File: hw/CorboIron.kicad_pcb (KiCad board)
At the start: 2 copper layers, 78.7 x 99.1 mm, 101 parts, among them P1 CONN_01X03, P10 CONN_01X04, P11 CONN_01X04, P2 CONN_01X03, P3 CONN_01X03, P4 Arduino_nano, P5 CONN_01X03, P6 CONN_01X04, P7 CONN_01X02, P8 CONN_01X03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

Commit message: Added descriptive text in silk
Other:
- board text added: "Four channel solder iron controller"
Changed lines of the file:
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@@
     (area 116.684238 56.84 211.2 163.905001)
     (thickness 1.6)
-    (drawings 29)
+    (drawings 30)
     (tracks 1597)
     (zones 0)
@@
   )
   (setup
-    (last_trace_width 0.3)
+    (last_trace_width 0.25)
     (user_trace_width 0.1524)
     (user_trace_width 0.3)
@@
     )
   )
+  (gr_text "Four channel \nsolder iron controller" (at 147.32 94.742) (layer F.SilkS)
+    (effects (font (size 1.5 1.5) (thickness 0.3)))
+  )
   (gr_text "LEDS INDICATE OVER HEAT PROTECTION" (at 139.7 161.798) (layer F.SilkS)

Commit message: Minor changes
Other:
- board text added: "1"
- board text added: "2"
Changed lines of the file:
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@@
     (area 116.684238 56.84 211.2 163.905001)
     (thickness 1.6)
-    (drawings 30)
-    (tracks 1597)
+    (drawings 32)
+    (tracks 1598)
     (zones 0)
     (modules 101)
@@
   (layers
     (0 F.Cu signal)
-    (31 B.Cu signal hide)
+    (31 B.Cu signal)
     (32 B.Adhes user)
     (33 F.Adhes user)
@@
   )
   (setup
-    (last_trace_width 0.25)
+    (last_trace_width 1)
     (user_trace_width 0.1524)
     (user_trace_width 0.3)
@@
     )
   )
+  (gr_text 2 (at 119.634 162.56) (layer B.Cu)
+    (effects (font (size 1.5 1.5) (thickness 0.3)))
+  )
+  (gr_text 1 (at 118.11 162.56) (layer F.Cu)
+    (effects (font (size 1.5 1.5) (thickness 0.3)))
+  )
   (gr_text "Four channel \nsolder iron controller" (at 147.32 94.742) (layer F.SilkS)
     (effects (font (size 1.5 1.5) (thickness 0.3)))
   )
-  (gr_text "LEDS INDICATE OVER HEAT PROTECTION" (at 139.7 161.798) (layer F.SilkS)
+  (gr_text "LEDS INDICATE OVER HEAT PROTECTION" (at 150.368 161.798) (layer F.SilkS)
     (effects (font (size 1.5 1.5) (thickness 0.3)))
   )
@@
   (via (at 131.445 142.621) (size 0.6) (drill 0.4) (layers F.Cu B.Cu) (net 1))
   (segment (start 129.286 142.621) (end 131.445 142.621) (width 0.7) (layer B.Cu) (net 1))
-  (segment (start 154.178 138.496) (end 154.178 133.223) (width 0.7) (layer F.Cu) (net 1))
-  (segment (start 148.717 131.191) (end 144.78 127.254) (width 0.7) (layer B.Cu) (net 1))
-  (segment (start 152.146 131.191) (end 148.717 131.191) (width 0.7) (layer B.Cu) (net 1))
-  (segment (start 154.178 133.223) (end 152.146 131.191) (width 0.7) (layer B.Cu) (net 1))
+  (segment (start 154.178 138.496) (end 154.178 135.636) (width 1) (layer F.Cu) (net 1))
   (via (at 154.178 133.223) (size 0.6) (drill 0.4) (layers F.Cu B.Cu) (net 1))
+  (segment (start 154.178 133.223) (end 152.146 131.191) (width 1) (layer B.Cu) (net 1))
+  (segment (start 152.146 131.191) (end 148.717 131.191) (width 1) (layer B.Cu) (net 1))
+  (segment (start 148.717 131.191) (end 144.78 127.254) (width 1) (layer B.Cu) (net 1))
+  (segment (start 154.178 135.636) (end 154.178 133.223) (width 0.7) (layer F.Cu) (net 1))
   (via (at 134.874 127.254) (size 0.6) (drill 0.4) (layers F.Cu B.Cu) (net 1))
   (segment (start 134.874 127.254) (end 134.874 131.572) (width 0.7) (layer B.Cu) (net 1))
@@
   (via (at 148.336 137.16) (size 0.6) (drill 0.4) (layers F.Cu B.Cu) (net 1))
   (segment (start 148.336 137.16) (end 148.27 137.16) (width 0.3) (layer F.Cu) (net 1))
-  (segment (start 153.538 138.496) (end 151.826 140.208) (width 0.7) (layer F.Cu) (net 1))
+  (segment (start 153.538 138.496) (end 151.826 140.208) (width 1) (layer F.Cu) (net 1))
   (via (at 151.826 140.208) (size 0.6) (drill 0.4) (layers F.Cu B.Cu) (net 1))
   (segment (start 151.826 140.208) (end 148.778 137.16) (width 0.3) (layer B.Cu) (net 1))
@@
     (polygon
       (pts
-        (xy 116.84 64.77) (xy 116.84 163.83) (xy 148.336 163.83) (xy 148.336 131.826) (xy 176.784 131.826)
-        (xy 176.784 163.83) (xy 195.58 163.83) (xy 195.58 64.77) (xy 176.784 64.77) (xy 176.784 95.504)
-        (xy 148.336 95.504) (xy 148.336 64.77)
+        (xy 116.84 64.77) (xy 116.84 160.782) (xy 120.65 160.782) (xy 120.65 163.83) (xy 148.336 163.83)
+        (xy 148.336 131.826) (xy 176.784 131.826) (xy 176.784 163.83) (xy 195.58 163.83) (xy 195.58 64.77)
+        (xy 176.784 64.77) (xy 176.784 95.504) (xy 148.336 95.504) (xy 148.336 64.77)
       )
     )

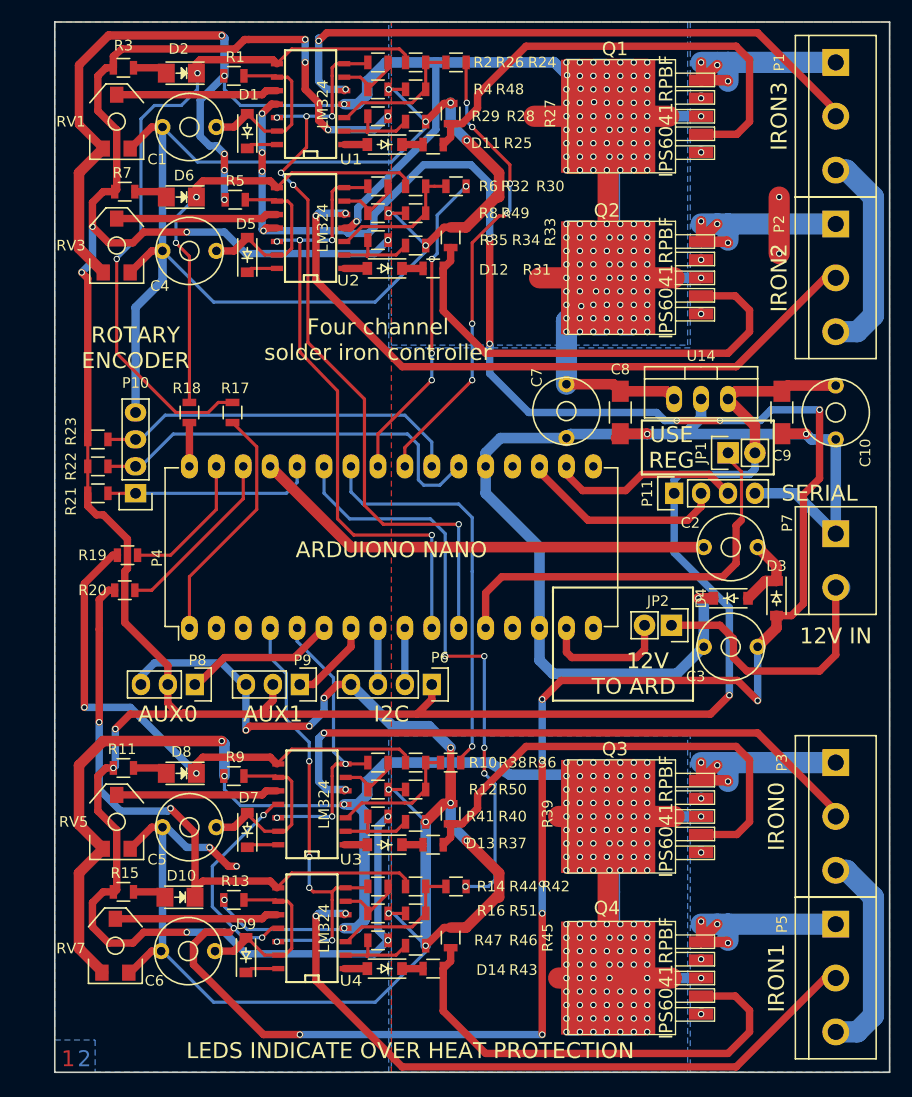
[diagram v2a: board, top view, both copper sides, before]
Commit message: Checked footprints, design should be ready for production
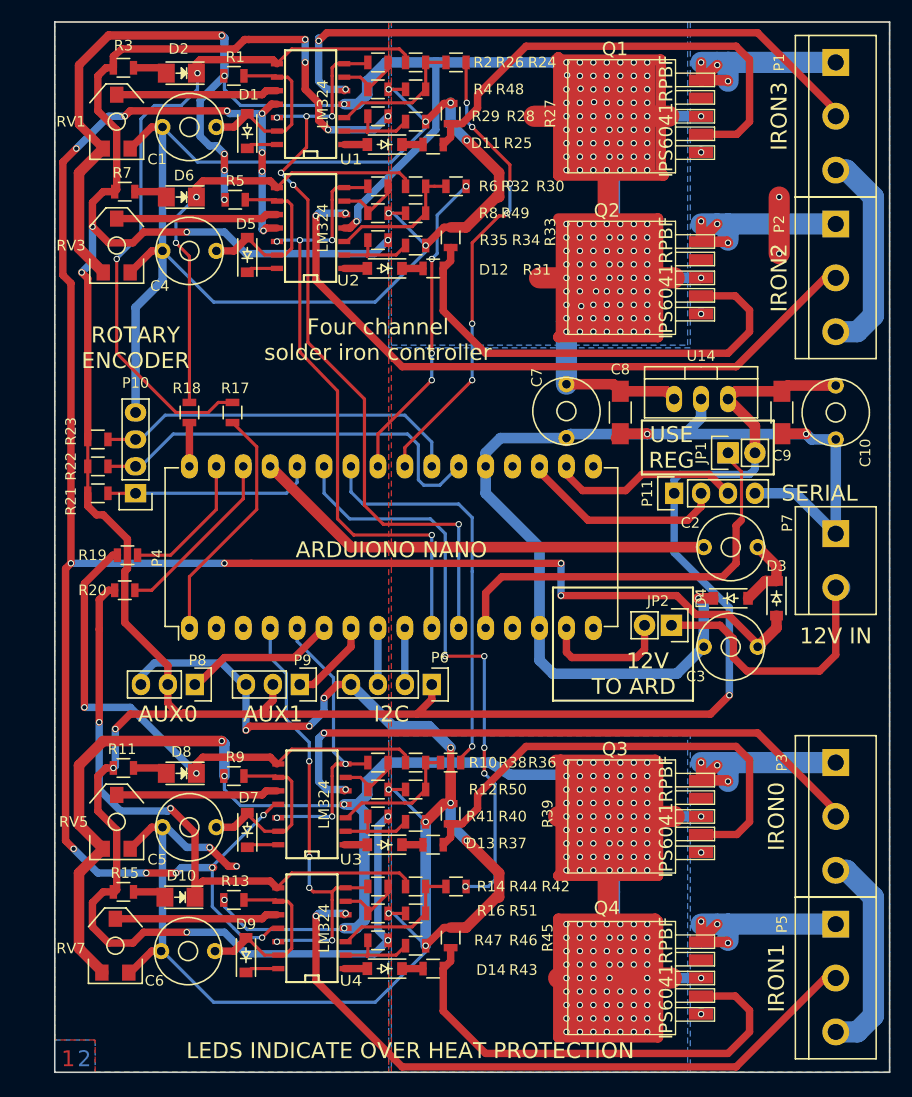
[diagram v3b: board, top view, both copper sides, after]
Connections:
- P4 pad 13: Net-(P4-Pad13) -> (no net)
- P4 pad 16: Net-(P4-Pad16) -> (no net)
- P4 pad 17: Net-(P4-Pad17) -> (no net)
- P4 pad 2: +3V3 -> (no net)
- P4 pad 20: Net-(P4-Pad20) -> (no net)
- P4 pad 3: /REF -> (no net)
- Q1 pad 4: GND -> (no net)
- Q3 pad 4: GND -> (no net)
- Q4 pad 4: GND -> (no net)
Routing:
- net +12V: track 770.7 -> 964.7 mm
- net /V_NEG: track 237.8 -> 209.0 mm, vias 19 -> 17
- net GND: track 426.6 -> 426.3 mm, vias 32 -> 28
- added copper zone on F.Cu, net GND
